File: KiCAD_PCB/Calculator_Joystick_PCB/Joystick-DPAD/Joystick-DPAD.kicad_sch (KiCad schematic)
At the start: 9 parts, among them SW1 SW_SPST, SW2 SW_SPST, SW3 SW_SPST, SW4 SW_SPST

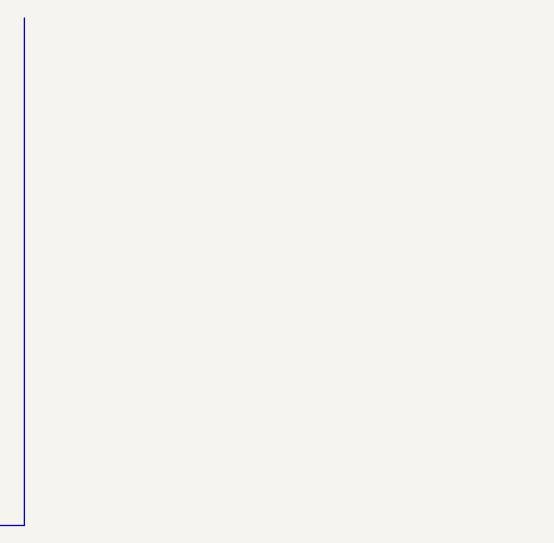
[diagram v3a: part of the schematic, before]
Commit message: JoyStick PCB Updates
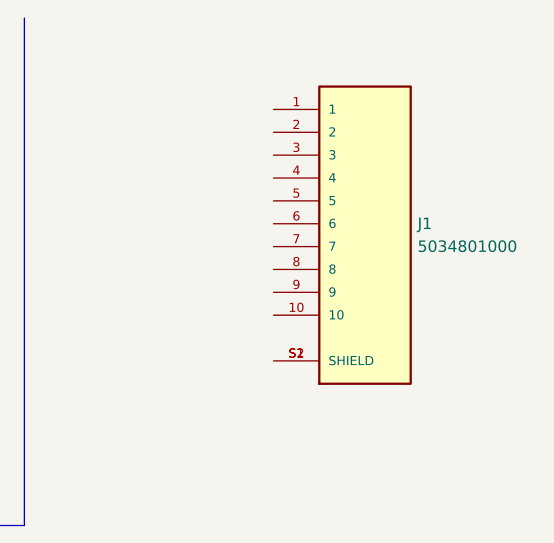
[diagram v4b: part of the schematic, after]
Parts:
- added J1: 5034801000, 5034801000:MOLEX_5034801000, symbol 5034801000:5034801000
- JOY1: footprint (none) -> Adafruit_Thumbstick:JOYSTICK_ANALOG_MINITHM
- SW1, SW2, SW3, SW4: footprint (none) -> KSA_Switch:KSA1M331LFT
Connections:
- new net: J1.S1 (SHIELD), J1.S2 (SHIELD)
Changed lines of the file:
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@@
     (property "Reference" "SW4" (id 0) (at 106.934 33.274 0))
     (property "Value" "SW_SPST" (id 1) (at 106.934 35.814 0))
-    (property "Footprint" "" (id 2) (at 106.934 40.386 0)
+    (property "Footprint" "KSA_Switch:KSA1M331LFT" (id 2) (at 106.934 40.386 0)
       (effects (font (size 1.27 1.27)) hide)
     )
@@
     (property "Reference" "SW3" (id 0) (at 87.122 44.958 0))
     (property "Value" "SW_SPST" (id 1) (at 87.122 47.498 0))
-    (property "Footprint" "" (id 2) (at 87.122 52.07 0)
+    (property "Footprint" "KSA_Switch:KSA1M331LFT" (id 2) (at 87.122 52.07 0)
       (effects (font (size 1.27 1.27)) hide)
     )
@@
       (effects (font (size 1.27 1.0795)) (justify left bottom))
     )
-    (property "Footprint" "" (id 2) (at 28.956 35.052 0)
+    (property "Footprint" "Adafruit_Thumbstick:JOYSTICK_ANALOG_MINITHM" (id 2) (at 28.956 35.052 0)
       (effects (font (size 1.27 1.27)) hide)
     )
@@
     (property "Reference" "SW2" (id 0) (at 87.122 21.59 0))
     (property "Value" "SW_SPST" (id 1) (at 87.122 24.13 0))
-    (property "Footprint" "" (id 2) (at 87.122 28.702 0)
+    (property "Footprint" "KSA_Switch:KSA1M331LFT" (id 2) (at 87.122 28.702 0)
       (effects (font (size 1.27 1.27)) hide)
     )
@@
       (effects (font (size 1.27 1.0795)) (justify left bottom))
     )
-    (property "Footprint" "" (id 2) (at 29.21 57.15 0)
+    (property "Footprint" "Adafruit_Thumbstick:JOYSTICK_ANALOG_MINITHM" (id 2) (at 29.21 57.15 0)
       (effects (font (size 1.27 1.27)) hide)
     )
@@
     (property "Reference" "SW1" (id 0) (at 67.31 33.274 0))
     (property "Value" "SW_SPST" (id 1) (at 67.31 35.814 0))
-    (property "Footprint" "" (id 2) (at 67.31 40.386 0)
+    (property "Footprint" "KSA_Switch:KSA1M331LFT" (id 2) (at 67.31 40.386 0)
       (effects (font (size 1.27 1.27)) hide)
     )
@@
     (pin "2")
   )
+  (symbol (lib_id "5034801000:5034801000") (at 153.924 37.338 0) (unit 1)
+    (in_bom yes) (on_board yes) (fields_autoplaced)
+    (property "Reference" "J1" (id 0) (at 159.766 34.7979 0)
+      (effects (font (size 1.27 1.27)) (justify left))
+    )
+    (property "Value" "5034801000" (id 1) (at 159.766 37.3379 0)
+      (effects (font (size 1.27 1.27)) (justify left))
+    )
+    (property "Footprint" "5034801000:MOLEX_5034801000" (id 2) (at 153.924 37.338 0)
+      (effects (font (size 1.27 1.27)) (justify left bottom) hide)
+    )
+    (property "Datasheet" "" (id 3) (at 153.924 37.338 0)
+      (effects (font (size 1.27 1.27)) (justify left bottom) hide)
+    )
+    (property "MANUFACTURER" "MOLEX" (id 4) (at 153.924 37.338 0)
+      (effects (font (size 1.27 1.27)) (justify left bottom) hide)
+    )
+    (property "STANDARD" "Manufacturer Recommendation" (id 5) (at 153.924 37.338 0)
+      (effects (font (size 1.27 1.27)) (justify left bottom) hide)
+    )
+    (property "PARTREV" "H" (id 6) (at 153.924 37.338 0)
+      (effects (font (size 1.27 1.27)) (justify left bottom) hide)
+    )
+    (pin "1")
+    (pin "10")
+    (pin "2")
+    (pin "3")
+    (pin "4")
+    (pin "5")
+    (pin "6")
+    (pin "7")
+    (pin "8")
+    (pin "9")
+    (pin "S1")
+    (pin "S2")
+  )
   (sheet_instances
     (path "/" (page "1"))
@@
       (reference "D4") (unit 1) (value "D_Small") (footprint "Diode_SMD:D_SOD-123")
     )
+    (path "/fb925c35-d58b-43d4-9440-2d680bd281dc"
+      (reference "J1") (unit 1) (value "5034801000") (footprint "5034801000:MOLEX_5034801000")
+    )
     (path "/3da07d8c-85c3-4a2f-a9bc-8b9585ef72db"

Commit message: V2 Updates
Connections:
- net XOUT is gone; now on net x_out: JOY1.X (S)
- net Col0: now also J1.5
- net Col1: now also J1.4
- net Col2: now also J1.3
- net GND: now also J1.S1 (SHIELD), J1.S2 (SHIELD)
- net y_out: now reaches J1.1
- net x_out: now reaches J1.2
- net Row3: now reaches J1.6
- net Row4: now reaches J1.7
- net Row5: now reaches J1.8
- no-connect marks 0 -> 2
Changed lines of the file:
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@@
   (junction (at 55.118 42.926) (diameter 0) (color 0 0 0 0)
   )
+  (no_connect (at 141.224 44.958))
+  (no_connect (at 141.224 42.418))
   (polyline (pts (xy 116.078 68.326) (xy 116.078 11.938))
     (stroke (width 0) (type default) (color 0 0 0 0))
@@
     (stroke (width 0) (type default) (color 0 0 0 0))
   )
+  (wire (pts (xy 141.224 39.878) (xy 143.764 39.878))
+    (stroke (width 0) (type default) (color 0 0 0 0))
+  )
   (wire (pts (xy 75.946 52.07) (xy 74.93 52.07))
     (stroke (width 0) (type default) (color 0 0 0 0))
   )
+  (wire (pts (xy 141.224 37.338) (xy 143.764 37.338))
+    (stroke (width 0) (type default) (color 0 0 0 0))
+  )
+  (wire (pts (xy 141.224 22.098) (xy 143.764 22.098))
+    (stroke (width 0) (type default) (color 0 0 0 0))
+  )
+  (wire (pts (xy 141.224 34.798) (xy 143.764 34.798))
+    (stroke (width 0) (type default) (color 0 0 0 0))
+  )
+  (wire (pts (xy 141.224 29.718) (xy 143.764 29.718))
+    (stroke (width 0) (type default) (color 0 0 0 0))
+  )
   (wire (pts (xy 81.026 52.07) (xy 82.042 52.07))
     (stroke (width 0) (type default) (color 0 0 0 0))
@@
     (stroke (width 0) (type default) (color 0 0 0 0))
   )
+  (wire (pts (xy 141.224 24.638) (xy 143.764 24.638))
+    (stroke (width 0) (type default) (color 0 0 0 0))
+  )
   (wire (pts (xy 74.93 28.702) (xy 74.93 31.242))
     (stroke (width 0) (type default) (color 0 0 0 0))
@@
     (stroke (width 0) (type default) (color 0 0 0 0))
   )
+  (wire (pts (xy 141.224 44.958) (xy 143.764 44.958))
+    (stroke (width 0) (type default) (color 0 0 0 0))
+  )
   (wire (pts (xy 56.134 40.386) (xy 55.118 40.386))
     (stroke (width 0) (type default) (color 0 0 0 0))
@@
     (stroke (width 0) (type default) (color 0 0 0 0))
   )
+  (wire (pts (xy 141.224 32.258) (xy 143.764 32.258))
+    (stroke (width 0) (type default) (color 0 0 0 0))
+  )
+  (wire (pts (xy 141.224 50.038) (xy 143.764 50.038))
+    (stroke (width 0) (type default) (color 0 0 0 0))
+  )
   (wire (pts (xy 72.39 18.288) (xy 72.39 40.386))
     (stroke (width 0) (type default) (color 0 0 0 0))
@@
     (stroke (width 0) (type default) (color 0 0 0 0))
   )
+  (wire (pts (xy 141.224 42.418) (xy 143.764 42.418))
+    (stroke (width 0) (type default) (color 0 0 0 0))
+  )
+  (wire (pts (xy 141.224 51.054) (xy 141.224 50.038))
+    (stroke (width 0) (type default) (color 0 0 0 0))
+  )
   (wire (pts (xy 100.838 40.386) (xy 101.854 40.386))
     (stroke (width 0) (type default) (color 0 0 0 0))
@@
   )
   (polyline (pts (xy 46.482 68.326) (xy 46.482 11.938))
+    (stroke (width 0) (type default) (color 0 0 0 0))
+  )
+  (wire (pts (xy 141.224 27.178) (xy 143.764 27.178))
     (stroke (width 0) (type default) (color 0 0 0 0))
   )
@@
     (effects (font (size 1.27 1.27)) (justify right bottom))
   )
-  (label "XOUT" (at 36.83 35.052 0)
+  (label "x_out" (at 36.83 35.052 0)
     (effects (font (size 1.2446 1.2446)) (justify left bottom))
   )
+  (label "Row4" (at 141.224 37.338 180)
+    (effects (font (size 1.27 1.27)) (justify right bottom))
+  )
+  (label "x_out" (at 141.224 24.638 180)
+    (effects (font (size 1.27 1.27)) (justify right bottom))
+  )
   (label "Row2" (at 52.578 54.61 180)
     (effects (font (size 1.27 1.27)) (justify right bottom))
   )
+  (label "y_out" (at 141.224 22.098 180)
+    (effects (font (size 1.27 1.27)) (justify right bottom))
+  )
+  (label "Row5" (at 141.224 39.878 180)
+    (effects (font (size 1.27 1.27)) (justify right bottom))
+  )
   (label "Row1" (at 52.578 31.242 180)
+    (effects (font (size 1.27 1.27)) (justify right bottom))
+  )
+  (label "Col0" (at 141.224 32.258 180)
     (effects (font (size 1.27 1.27)) (justify right bottom))
   )
   (label "YOUT" (at 36.83 57.15 0)
     (effects (font (size 1.2446 1.2446)) (justify left bottom))
+  )
+  (label "Row3" (at 141.224 34.798 180)
+    (effects (font (size 1.27 1.27)) (justify right bottom))
+  )
+  (label "Col2" (at 141.224 27.178 180)
+    (effects (font (size 1.27 1.27)) (justify right bottom))
+  )
+  (label "Col1" (at 141.224 29.718 180)
+    (effects (font (size 1.27 1.27)) (justify right bottom))
   )
   (label "Col0" (at 72.39 18.288 180)
@@
     (pin "S2")
   )
+  (symbol (lib_id "power:GND") (at 141.224 51.054 0) (unit 1)
+    (in_bom yes) (on_board yes) (fields_autoplaced)
+    (property "Reference" "#PWR0101" (id 0) (at 141.224 57.404 0)
+      (effects (font (size 1.27 1.27)) hide)
+    )
+    (property "Value" "GND" (id 1) (at 141.224 55.626 0))
+    (property "Footprint" "" (id 2) (at 141.224 51.054 0)
+      (effects (font (size 1.27 1.27)) hide)
+    )
+    (property "Datasheet" "" (id 3) (at 141.224 51.054 0)
+      (effects (font (size 1.27 1.27)) hide)
+    )
+    (pin "1")
+  )
   (sheet_instances
     (path "/" (page "1"))
@@
       (reference "#GND0102") (unit 1) (value "GND") (footprint "Adafruit Mini Analog Thumbstick:")
     )
+    (path "/fee09553-ca13-4e5a-b7ad-f447e7c207ea"
+      (reference "#PWR0101") (unit 1) (value "GND") (footprint "")
+    )
     (path "/66553eac-3edc-435c-bc67-3973452c2abb"

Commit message: V2 Updates
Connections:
- net Row1 is gone; now on net Row3: D2.1 (K)
- net YOUT is gone; now on net y_out: JOY1.Y (S)
- net Row4: now also D1.1 (K), D4.1 (K)
- net Row5: now also D3.1 (K)
- removed net Row2: D1.1 (K), D3.1 (K), D4.1 (K)
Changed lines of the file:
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@@
     (effects (font (size 1.27 1.27)) (justify right bottom))
   )
-  (label "Row2" (at 52.578 54.61 180)
+  (label "Row5" (at 52.578 54.61 180)
     (effects (font (size 1.27 1.27)) (justify right bottom))
   )
@@
     (effects (font (size 1.27 1.27)) (justify right bottom))
   )
-  (label "Row1" (at 52.578 31.242 180)
+  (label "Row3" (at 52.578 31.242 180)
     (effects (font (size 1.27 1.27)) (justify right bottom))
   )
@@
     (effects (font (size 1.27 1.27)) (justify right bottom))
   )
-  (label "YOUT" (at 36.83 57.15 0)
+  (label "y_out" (at 36.83 57.15 0)
     (effects (font (size 1.2446 1.2446)) (justify left bottom))
   )
@@
     (effects (font (size 1.27 1.27)) (justify right bottom))
   )
-  (label "Row2" (at 52.578 42.926 180)
+  (label "Row4" (at 52.578 42.926 180)
     (effects (font (size 1.27 1.27)) (justify right bottom))
   )
